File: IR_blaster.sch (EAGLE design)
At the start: 54 parts, among them J2 Micro USB, J3 Mini USB, J4 nRF24L01+, J5 FTDI, Q1IL1 BC337, Q1IL2 BC337, Q1IL3 BC337, Q1IL4 BC337, SW1P SPDT_SWITCH_2MM

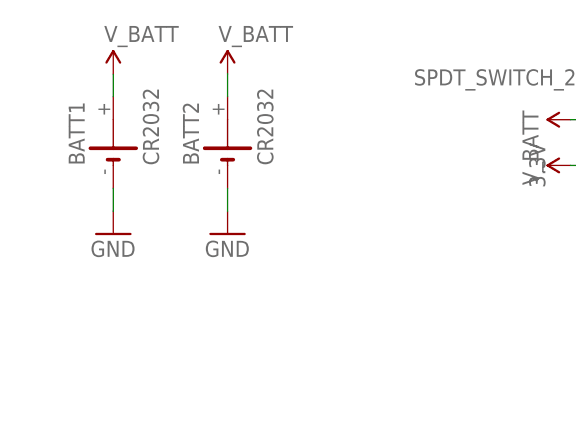
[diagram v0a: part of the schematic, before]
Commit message: Changed the batteries packages to double pin ones.
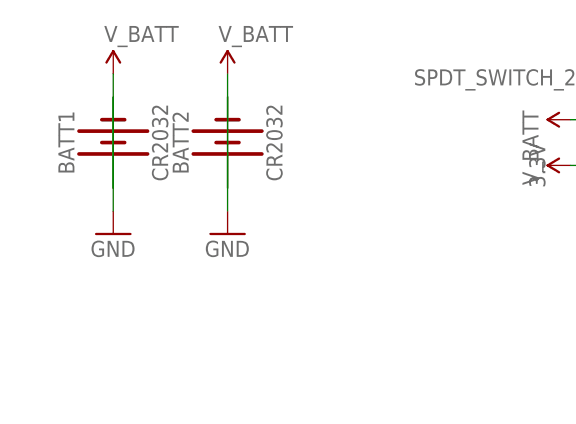
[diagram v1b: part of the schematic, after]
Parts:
- BATT1, BATT2: device battery:CR2032H -> SparkFun-Batteries:BATTERY-20MM_PTH
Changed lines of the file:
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@@
 <grid distance="0.1" unitdist="inch" unit="inch" style="lines" multiple="1" display="no" altdistance="0.01" altunitdist="inch" altunit="inch"/>
 <layers>
-<layer number="1" name="Top" color="4" fill="1" visible="no" active="no"/>
-<layer number="16" name="Bottom" color="1" fill="1" visible="no" active="no"/>
-<layer number="17" name="Pads" color="2" fill="1" visible="no" active="no"/>
-<layer number="18" name="Vias" color="2" fill="1" visible="no" active="no"/>
-<layer number="19" name="Unrouted" color="6" fill="1" visible="no" active="no"/>
-<layer number="20" name="Dimension" color="15" fill="1" visible="no" active="no"/>
-<layer number="21" name="tPlace" color="7" fill="1" visible="no" active="no"/>
-<layer number="22" name="bPlace" color="7" fill="1" visible="no" active="no"/>
-<layer number="23" name="tOrigins" color="15" fill="1" visible="no" active="no"/>
-<layer number="24" name="bOrigins" color="15" fill="1" visible="no" active="no"/>
-<layer number="25" name="tNames" color="7" fill="1" visible="no" active="no"/>
-<layer number="26" name="bNames" color="7" fill="1" visible="no" active="no"/>
-<layer number="27" name="tValues" color="7" fill="1" visible="no" active="no"/>
-<layer number="28" name="bValues" color="7" fill="1" visible="no" active="no"/>
+<layer number="1" name="Top" color="4" fill="1" visible="yes" active="no"/>
+<layer number="16" name="Bottom" color="1" fill="1" visible="yes" active="no"/>
+<layer number="17" name="Pads" color="2" fill="1" visible="yes" active="no"/>
+<layer number="18" name="Vias" color="2" fill="1" visible="yes" active="no"/>
+<layer number="19" name="Unrouted" color="6" fill="1" visible="yes" active="no"/>
+<layer number="20" name="Dimension" color="15" fill="1" visible="yes" active="no"/>
+<layer number="21" name="tPlace" color="7" fill="1" visible="yes" active="no"/>
+<layer number="22" name="bPlace" color="7" fill="1" visible="yes" active="no"/>
+<layer number="23" name="tOrigins" color="15" fill="1" visible="yes" active="no"/>
+<layer number="24" name="bOrigins" color="15" fill="1" visible="yes" active="no"/>
+<layer number="25" name="tNames" color="7" fill="1" visible="yes" active="no"/>
+<layer number="26" name="bNames" color="7" fill="1" visible="yes" active="no"/>
+<layer number="27" name="tValues" color="7" fill="1" visible="yes" active="no"/>
+<layer number="28" name="bValues" color="7" fill="1" visible="yes" active="no"/>
 <layer number="29" name="tStop" color="7" fill="3" visible="no" active="no"/>
 <layer number="30" name="bStop" color="7" fill="6" visible="no" active="no"/>
@@
 <layer number="35" name="tGlue" color="7" fill="4" visible="no" active="no"/>
 <layer number="36" name="bGlue" color="7" fill="5" visible="no" active="no"/>
-<layer number="37" name="tTest" color="7" fill="1" visible="no" active="no"/>
-<layer number="38" name="bTest" color="7" fill="1" visible="no" active="no"/>
+<layer number="37" name="tTest" color="7" fill="1" visible="yes" active="no"/>
+<layer number="38" name="bTest" color="7" fill="1" visible="yes" active="no"/>
 <layer number="39" name="tKeepout" color="4" fill="11" visible="no" active="no"/>
 <layer number="40" name="bKeepout" color="1" fill="11" visible="no" active="no"/>
@@
 <layer number="44" name="Drills" color="7" fill="1" visible="no" active="no"/>
 <layer number="45" name="Holes" color="7" fill="1" visible="no" active="no"/>
-<layer number="46" name="Milling" color="3" fill="1" visible="no" active="no"/>
-<layer number="47" name="Measures" color="7" fill="1" visible="no" active="no"/>
-<layer number="48" name="Document" color="7" fill="1" visible="no" active="no"/>
-<layer number="49" name="Reference" color="7" fill="1" visible="no" active="no"/>
-<layer number="50" name="dxf" color="7" fill="1" visible="no" active="no"/>
-<layer number="51" name="tDocu" color="7" fill="1" visible="no" active="no"/>
-<layer number="52" name="bDocu" color="7" fill="1" visible="no" active="no"/>
-<layer number="53" name="tGND_GNDA" color="7" fill="9" visible="no" active="no"/>
-<layer number="54" name="bGND_GNDA" color="1" fill="9" visible="no" active="no"/>
-<layer number="56" name="wert" color="7" fill="1" visible="no" active="no"/>
-<layer number="57" name="tCAD" color="7" fill="1" visible="no" active="no"/>
-<layer number="59" name="tCarbon" color="7" fill="1" visible="no" active="no"/>
-<layer number="60" name="bCarbon" color="7" fill="1" visible="no" active="no"/>
+<layer number="46" name="Milling" color="3" fill="1" visible="yes" active="no"/>
+<layer number="47" name="Measures" color="7" fill="1" visible="yes" active="no"/>
+<layer number="48" name="Document" color="7" fill="1" visible="yes" active="no"/>
+<layer number="49" name="Reference" color="7" fill="1" visible="yes" active="no"/>
+<layer number="50" name="dxf" color="7" fill="1" visible="yes" active="no"/>
+<layer number="51" name="tDocu" color="7" fill="1" visible="yes" active="no"/>
+<layer number="52" name="bDocu" color="7" fill="1" visible="yes" active="no"/>
+<layer number="53" name="tGND_GNDA" color="7" fill="9" visible="yes" active="no"/>
+<layer number="54" name="bGND_GNDA" color="1" fill="9" visible="yes" active="no"/>
+<layer number="56" name="wert" color="7" fill="1" visible="yes" active="no"/>
+<layer number="57" name="tCAD" color="7" fill="1" visible="yes" active="no"/>
+<layer number="59" name="tCarbon" color="7" fill="1" visible="yes" active="no"/>
+<layer number="60" name="bCarbon" color="7" fill="1" visible="yes" active="no"/>
 <layer number="90" name="Modules" color="5" fill="1" visible="yes" active="yes"/>
 <layer number="91" name="Nets" color="2" fill="1" visible="yes" active="yes"/>
@@
 </classes>
 <parts>
-<part name="BATT1" library="battery" deviceset="CR2032H" device="" value="CR2032"/>
+<part name="BATT1" library="SparkFun-Batteries" deviceset="BATTERY" device="-20MM_PTH" value="CR2032"/>
 <part name="GND1" library="SparkFun-Aesthetics" deviceset="GND" device=""/>
-<part name="BATT2" library="battery" deviceset="CR2032H" device="" value="CR2032"/>
+<part name="BATT2" library="SparkFun-Batteries" deviceset="BATTERY" device="-20MM_PTH" value="CR2032"/>
 <part name="GND3" library="SparkFun-Aesthetics" deviceset="GND" device=""/>
 <part name="SUPPLY15" library="SparkFun-Aesthetics" deviceset="V_BATT" device=""/>
@@
 </plain>
 <instances>
-<instance part="BATT1" gate="1" x="15.24" y="160.02" rot="R90"/>
+<instance part="BATT1" gate="G$1" x="15.24" y="160.02" rot="R90"/>
 <instance part="GND1" gate="1" x="15.24" y="149.86"/>
-<instance part="BATT2" gate="1" x="27.94" y="160.02" rot="R90"/>
+<instance part="BATT2" gate="G$1" x="27.94" y="160.02" rot="R90"/>
 <instance part="GND3" gate="1" x="27.94" y="149.86"/>
 <instance part="SUPPLY15" gate="G$1" x="15.24" y="167.64"/>
@@
 <segment>
 <pinref part="GND1" gate="1" pin="GND"/>
-<pinref part="BATT1" gate="1" pin="-"/>
-<wire x1="15.24" y1="152.4" x2="15.24" y2="154.94" width="0.1524" layer="91"/>
+<pinref part="BATT1" gate="G$1" pin="-"/>
+<wire x1="15.24" y1="152.4" x2="15.24" y2="165.1" width="0.1524" layer="91"/>
 </segment>
 <segment>
 <pinref part="GND3" gate="1" pin="GND"/>
-<pinref part="BATT2" gate="1" pin="-"/>
-<wire x1="27.94" y1="152.4" x2="27.94" y2="154.94" width="0.1524" layer="91"/>
+<pinref part="BATT2" gate="G$1" pin="-"/>
+<wire x1="27.94" y1="152.4" x2="27.94" y2="165.1" width="0.1524" layer="91"/>
 </segment>
 <segment>
@@
 <net name="V_BATT" class="0">
 <segment>
-<pinref part="BATT1" gate="1" pin="+"/>
-<wire x1="15.24" y1="165.1" x2="15.24" y2="167.64" width="0.1524" layer="91"/>
+<pinref part="BATT1" gate="G$1" pin="+"/>
+<wire x1="15.24" y1="154.94" x2="15.24" y2="167.64" width="0.1524" layer="91"/>
 <pinref part="SUPPLY15" gate="G$1" pin="V_BATT"/>
 </segment>
 <segment>
-<pinref part="BATT2" gate="1" pin="+"/>
+<pinref part="BATT2" gate="G$1" pin="+"/>
 <pinref part="SUPPLY1" gate="G$1" pin="V_BATT"/>
-<wire x1="27.94" y1="165.1" x2="27.94" y2="167.64" width="0.1524" layer="91"/>
-</segment>
-<segment>
+<wire x1="27.94" y1="154.94" x2="27.94" y2="167.64" width="0.1524" layer="91"/>
+</segment>
+<segment>

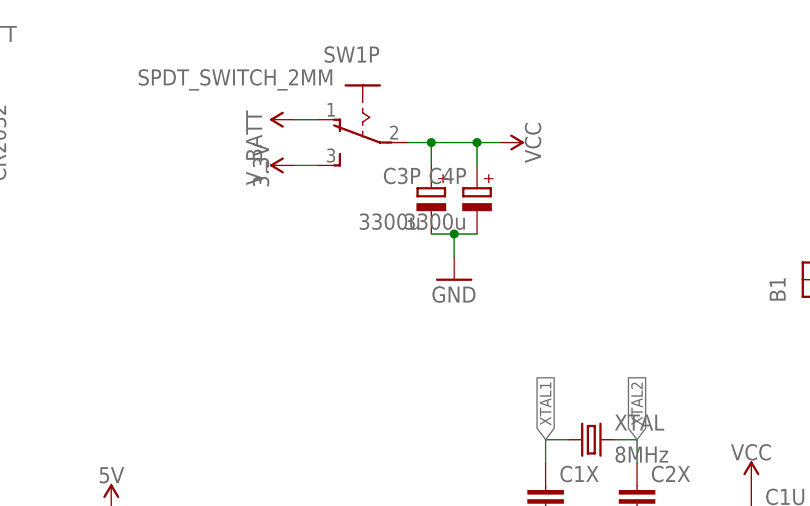
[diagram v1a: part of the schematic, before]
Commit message: Changed to smaller capacitors
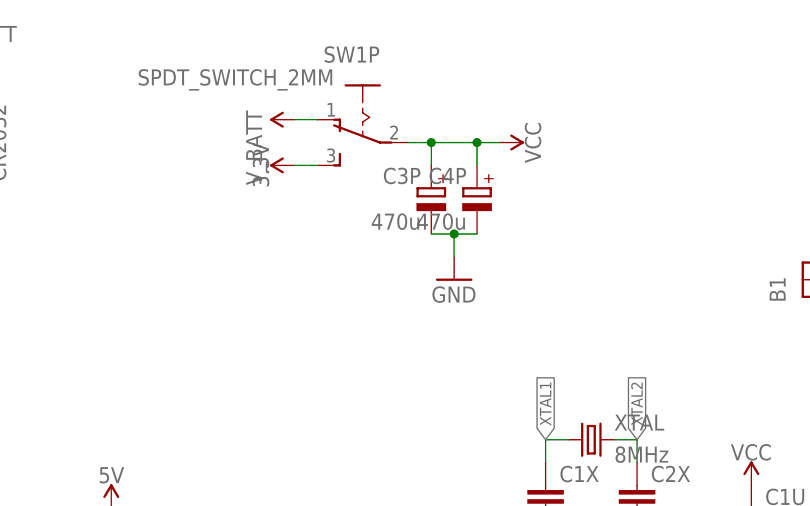
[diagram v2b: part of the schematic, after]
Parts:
- C3P, C4P: value 3300u -> 470u; device resistor:CPOL-EUE5-13 -> resistor:CPOL-EUE5-8.5
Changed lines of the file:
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@@
 <part name="R1P" library="resistor" deviceset="R-EU_" device="0207/7"/>
 <part name="GND7" library="SparkFun-Aesthetics" deviceset="GND" device=""/>
-<part name="C3P" library="resistor" deviceset="CPOL-EU" device="E5-13" value="3300u"/>
+<part name="C3P" library="resistor" deviceset="CPOL-EU" device="E5-8.5" value="470u"/>
 <part name="GND8" library="SparkFun-Aesthetics" deviceset="GND" device=""/>
 <part name="C1N" library="resistor" deviceset="C-EU" device="025-025X050" value="100n"/>
@@
 <part name="GND21" library="SparkFun-Aesthetics" deviceset="GND" device=""/>
 <part name="GND22" library="SparkFun-Aesthetics" deviceset="GND" device=""/>
-<part name="C4P" library="resistor" deviceset="CPOL-EU" device="E5-13" value="3300u"/>
+<part name="C4P" library="resistor" deviceset="CPOL-EU" device="E5-8.5" value="470u"/>
 <part name="R1BATT" library="resistor" deviceset="R-EU_" device="0207/7" value="20k"/>
 <part name="R2BATT" library="resistor" deviceset="R-EU_" device="0207/7" value="10k"/>
